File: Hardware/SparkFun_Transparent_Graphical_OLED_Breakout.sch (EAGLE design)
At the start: 35 parts, among them U1 AP3012, U2 UG-2856KLBAG01_4WSPI

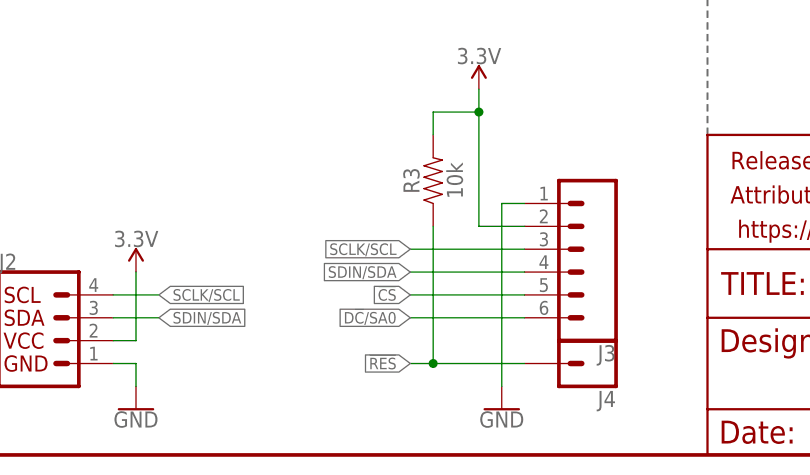
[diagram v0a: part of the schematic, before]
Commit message: Add capacitor to reset line for delayed start up!
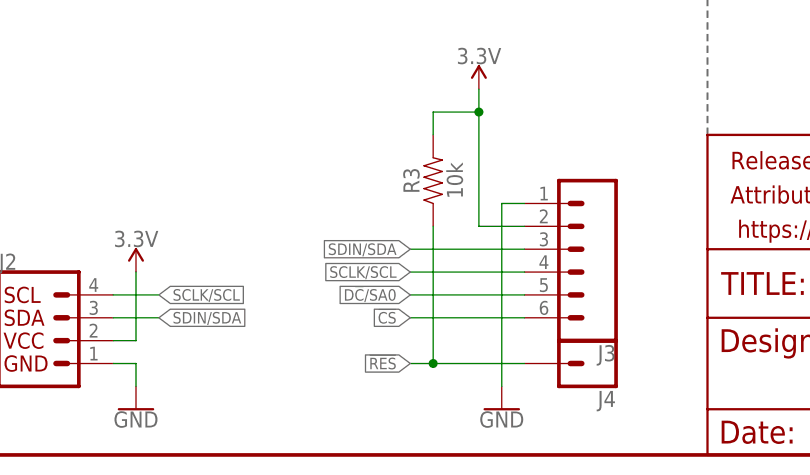
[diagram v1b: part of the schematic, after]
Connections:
- net !CS: now also J3.6; no longer J3.5
- net D!C!/SA0: now also J3.5; no longer J3.6
- net SCLK/SCL: now also J3.4; no longer J3.3
- net SDIN/SDA: now also J3.3; no longer J3.4
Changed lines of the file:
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@@
 </segment>
 <segment>
-<label x="114.3" y="17.78" size="1.27" layer="95" rot="R180" xref="yes"/>
-<pinref part="J3" gate="G$1" pin="5"/>
-<wire x1="127" y1="17.78" x2="114.3" y2="17.78" width="0.1524" layer="91"/>
+<label x="114.3" y="15.24" size="1.27" layer="95" rot="R180" xref="yes"/>
+<wire x1="127" y1="15.24" x2="114.3" y2="15.24" width="0.1524" layer="91"/>
+<pinref part="J3" gate="G$1" pin="6"/>
 </segment>
 </net>
@@
 </segment>
 <segment>
-<label x="114.3" y="22.86" size="1.27" layer="95" rot="R180" xref="yes"/>
-<pinref part="J3" gate="G$1" pin="3"/>
-<wire x1="127" y1="22.86" x2="114.3" y2="22.86" width="0.1524" layer="91"/>
+<label x="114.3" y="20.32" size="1.27" layer="95" rot="R180" xref="yes"/>
+<wire x1="127" y1="20.32" x2="114.3" y2="20.32" width="0.1524" layer="91"/>
+<pinref part="J3" gate="G$1" pin="4"/>
 </segment>
 </net>
@@
 </segment>
 <segment>
-<label x="114.3" y="20.32" size="1.27" layer="95" rot="R180" xref="yes"/>
-<pinref part="J3" gate="G$1" pin="4"/>
-<wire x1="127" y1="20.32" x2="114.3" y2="20.32" width="0.1524" layer="91"/>
+<label x="114.3" y="22.86" size="1.27" layer="95" rot="R180" xref="yes"/>
+<wire x1="127" y1="22.86" x2="114.3" y2="22.86" width="0.1524" layer="91"/>
+<pinref part="J3" gate="G$1" pin="3"/>
 </segment>
 </net>
@@
 </segment>
 <segment>
-<label x="114.3" y="15.24" size="1.27" layer="95" rot="R180" xref="yes"/>
-<pinref part="J3" gate="G$1" pin="6"/>
-<wire x1="114.3" y1="15.24" x2="127" y2="15.24" width="0.1524" layer="91"/>
+<label x="114.3" y="17.78" size="1.27" layer="95" rot="R180" xref="yes"/>
+<wire x1="114.3" y1="17.78" x2="127" y2="17.78" width="0.1524" layer="91"/>
+<pinref part="J3" gate="G$1" pin="5"/>
 </segment>
 </net>

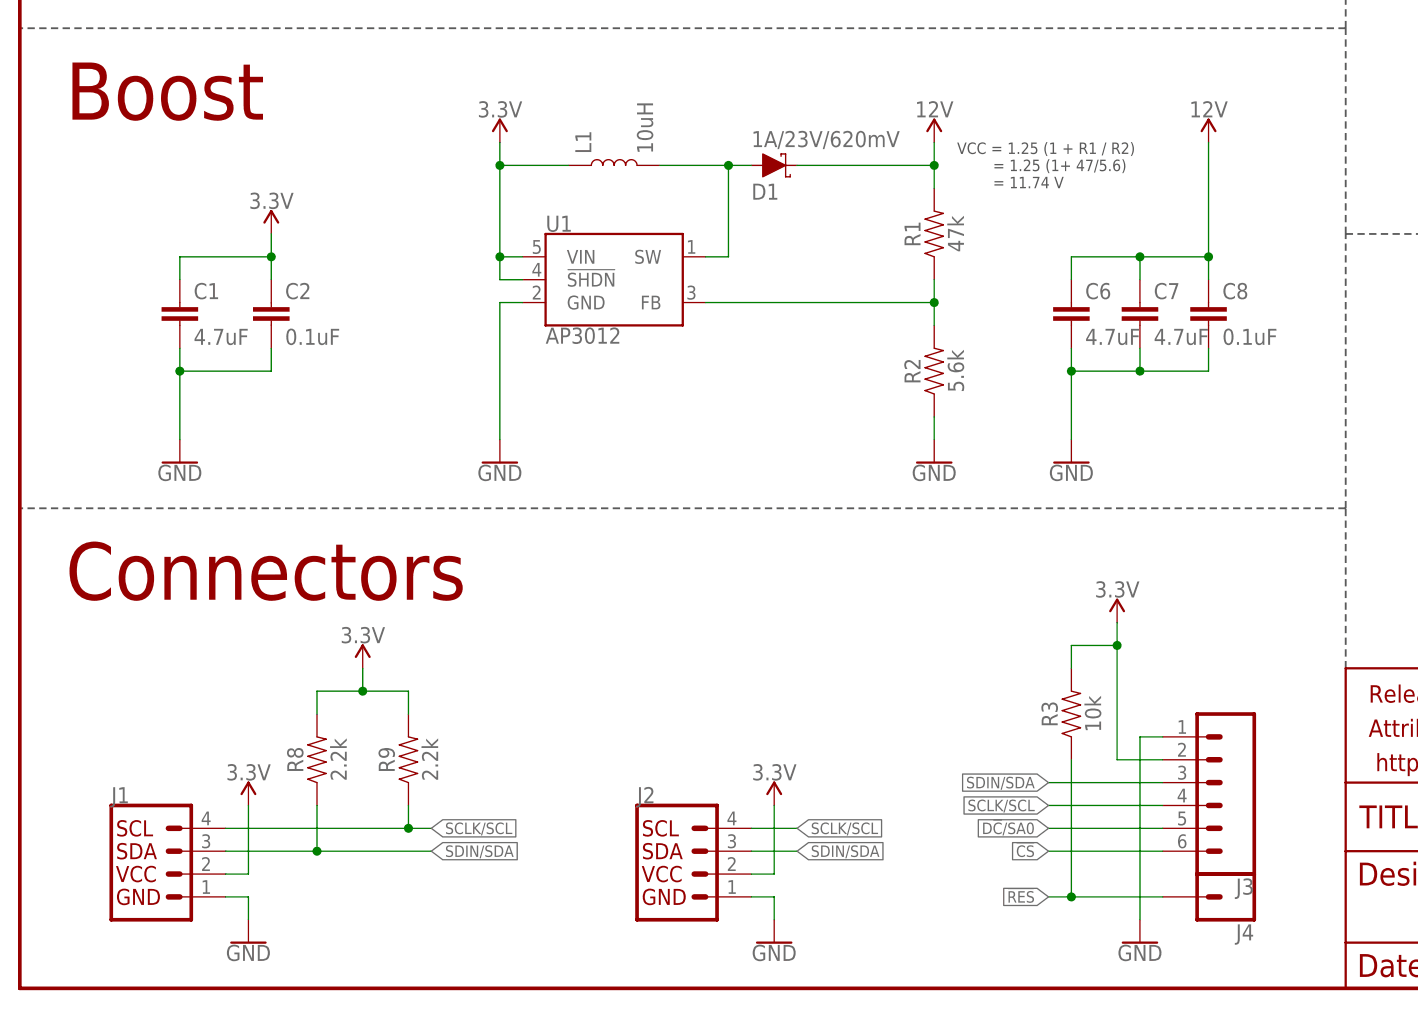
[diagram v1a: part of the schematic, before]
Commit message: Fixed proto issues
Added I2C pullup resistors and disconnect jumper, added power LED, added reset timing capacitor
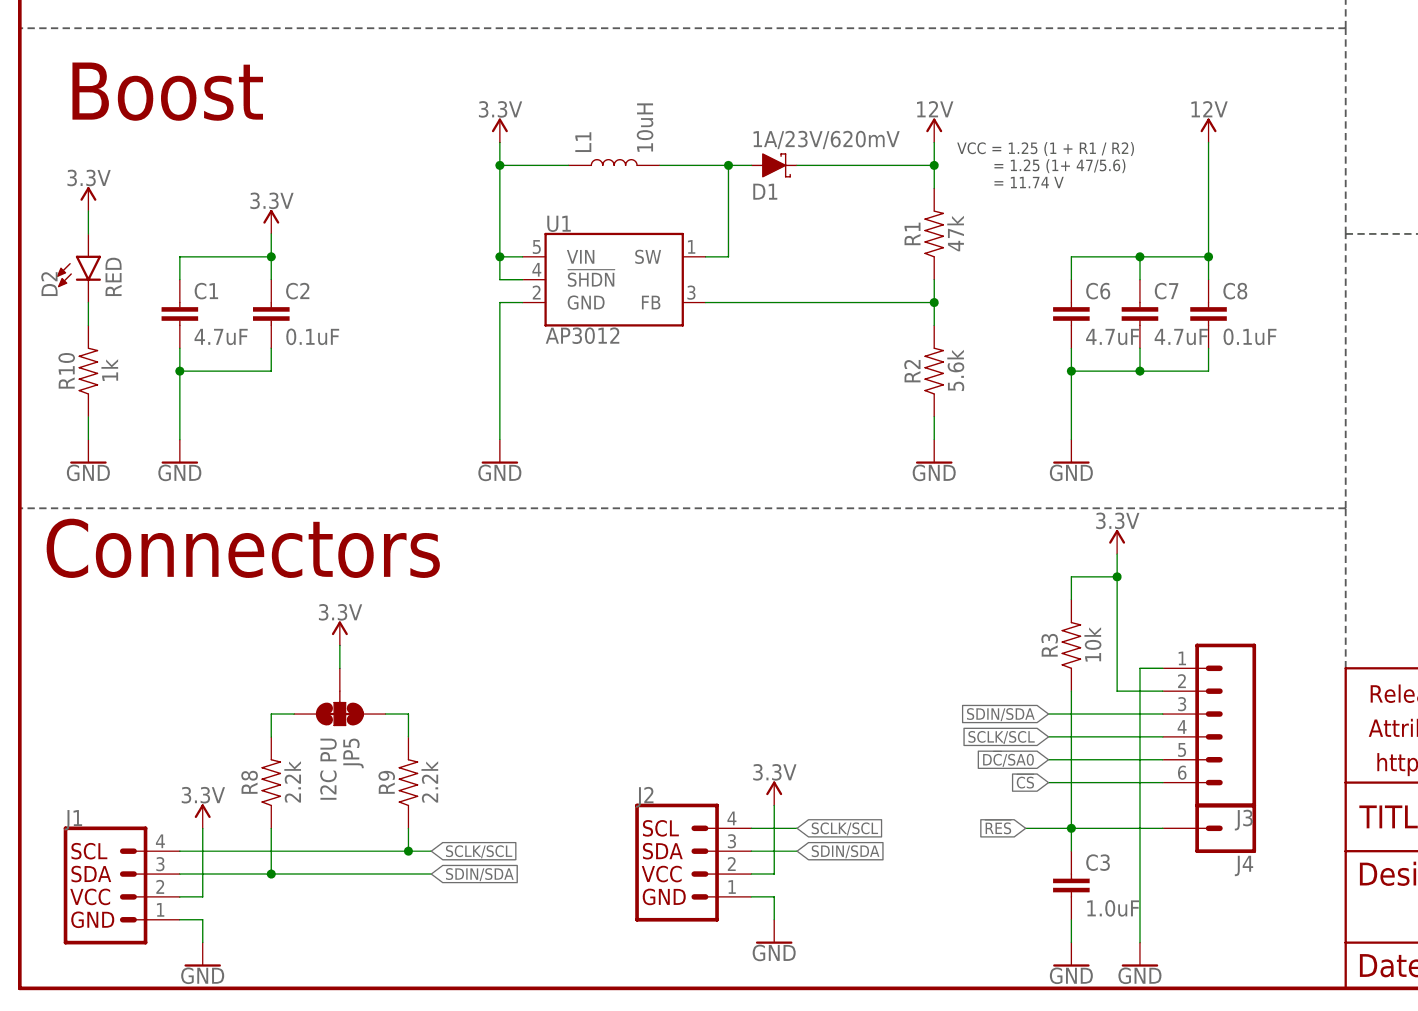
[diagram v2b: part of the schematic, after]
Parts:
- added C3: 1.0uF, SparkFun-Capacitors:1.0UF-0603-16V-10%-X7R
- added D2: RED, SparkFun-LED:LED-RED0603
- added JP5: I2C PU, SparkFun-Jumpers:JUMPER-SMT_3_2-NC_TRACE_SILK
- added R10: 1k, SparkFun-Resistors:1KOHM-0603-1/10W-1%
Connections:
- new net N$2: D2.C, R10.2
- new net N$6: JP5.3, R8.2
- new net N$7: JP5.1, R9.2
- net !RES: now also C3.1
- net 3.3V: now also D2.A, JP5.2; no longer R8.2, R9.2
- net GND: now also C3.2, R10.1
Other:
- moved on the sheet: J1, J3, J4, R3, R8, R9

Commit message: Tidy schematic
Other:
- moved on the sheet: C3
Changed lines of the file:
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@@
 <instance part="R9" gate="G$1" x="43.18" y="22.86" rot="R90"/>
 <instance part="SUPPLY13" gate="G$1" x="35.56" y="38.1"/>
-<instance part="C3" gate="G$1" x="116.84" y="10.16"/>
-<instance part="GND3" gate="1" x="116.84" y="2.54"/>
+<instance part="C3" gate="G$1" x="114.3" y="10.16"/>
+<instance part="GND3" gate="1" x="114.3" y="2.54"/>
 <instance part="D2" gate="G$1" x="7.62" y="81.28"/>
 <instance part="GND9" gate="1" x="7.62" y="58.42"/>
@@
 <pinref part="GND3" gate="1" pin="GND"/>
 <pinref part="C3" gate="G$1" pin="2"/>
-<wire x1="116.84" y1="5.08" x2="116.84" y2="7.62" width="0.1524" layer="91"/>
+<wire x1="114.3" y1="5.08" x2="114.3" y2="7.62" width="0.1524" layer="91"/>
 </segment>
 <segment>
@@
 <segment>
 <label x="111.76" y="17.78" size="1.27" layer="95" rot="R180" xref="yes"/>
-<wire x1="116.84" y1="17.78" x2="111.76" y2="17.78" width="0.1524" layer="91"/>
+<wire x1="116.84" y1="17.78" x2="114.3" y2="17.78" width="0.1524" layer="91"/>
 <pinref part="R3" gate="G$1" pin="1"/>
+<wire x1="114.3" y1="17.78" x2="111.76" y2="17.78" width="0.1524" layer="91"/>
 <wire x1="116.84" y1="33.02" x2="116.84" y2="17.78" width="0.1524" layer="91"/>
 <wire x1="116.84" y1="17.78" x2="127" y2="17.78" width="0.1524" layer="91"/>
@@
 <pinref part="J4" gate="G$1" pin="1"/>
 <pinref part="C3" gate="G$1" pin="1"/>
-<wire x1="116.84" y1="15.24" x2="116.84" y2="17.78" width="0.1524" layer="91"/>
+<wire x1="114.3" y1="15.24" x2="114.3" y2="17.78" width="0.1524" layer="91"/>
+<junction x="114.3" y="17.78"/>
 </segment>
 </net>
@@
 </segment>
 <segment>
-<label x="114.3" y="22.86" size="1.27" layer="95" rot="R180" xref="yes"/>
-<wire x1="127" y1="22.86" x2="114.3" y2="22.86" width="0.1524" layer="91"/>
+<label x="111.76" y="22.86" size="1.27" layer="95" rot="R180" xref="yes"/>
+<wire x1="127" y1="22.86" x2="111.76" y2="22.86" width="0.1524" layer="91"/>
 <pinref part="J3" gate="G$1" pin="6"/>
 </segment>
@@
 </segment>
 <segment>
-<label x="114.3" y="27.94" size="1.27" layer="95" rot="R180" xref="yes"/>
-<wire x1="127" y1="27.94" x2="114.3" y2="27.94" width="0.1524" layer="91"/>
+<label x="111.76" y="27.94" size="1.27" layer="95" rot="R180" xref="yes"/>
+<wire x1="127" y1="27.94" x2="111.76" y2="27.94" width="0.1524" layer="91"/>
 <pinref part="J3" gate="G$1" pin="4"/>
 </segment>
@@
 </segment>
 <segment>
-<label x="114.3" y="30.48" size="1.27" layer="95" rot="R180" xref="yes"/>
-<wire x1="127" y1="30.48" x2="114.3" y2="30.48" width="0.1524" layer="91"/>
+<label x="111.76" y="30.48" size="1.27" layer="95" rot="R180" xref="yes"/>
+<wire x1="127" y1="30.48" x2="111.76" y2="30.48" width="0.1524" layer="91"/>
 <pinref part="J3" gate="G$1" pin="3"/>
 </segment>
@@
 </segment>
 <segment>
-<label x="114.3" y="25.4" size="1.27" layer="95" rot="R180" xref="yes"/>
-<wire x1="114.3" y1="25.4" x2="127" y2="25.4" width="0.1524" layer="91"/>
+<label x="111.76" y="25.4" size="1.27" layer="95" rot="R180" xref="yes"/>
+<wire x1="111.76" y1="25.4" x2="127" y2="25.4" width="0.1524" layer="91"/>
 <pinref part="J3" gate="G$1" pin="5"/>
 </segment>

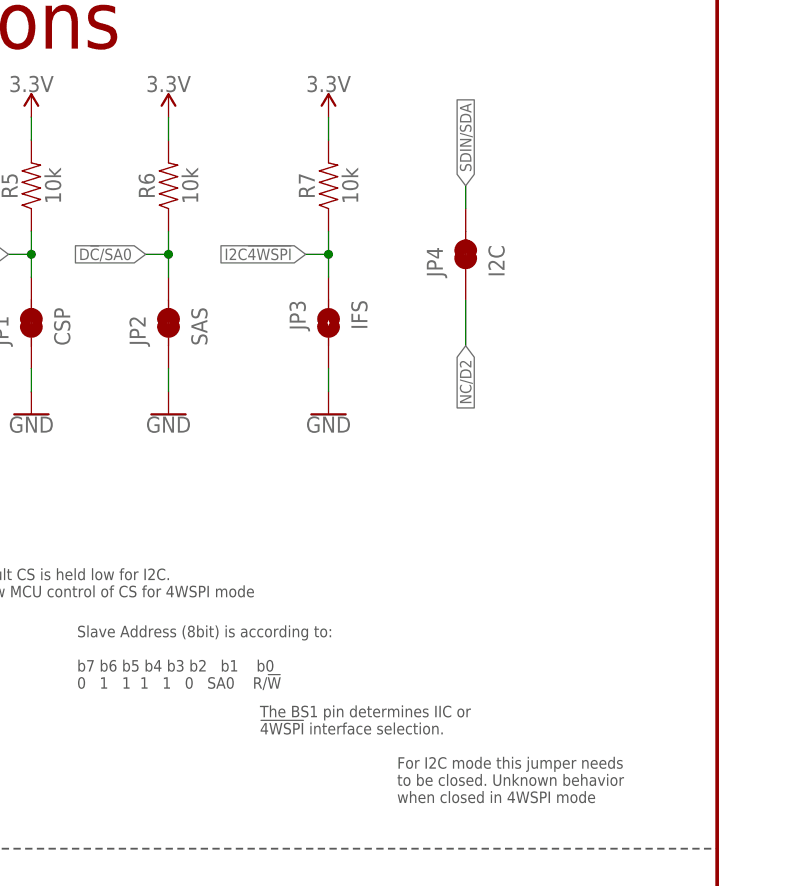
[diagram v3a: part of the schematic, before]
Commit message: Changed polarity of IFS jumper so that changing to SPI is all cutting, changed silk to match
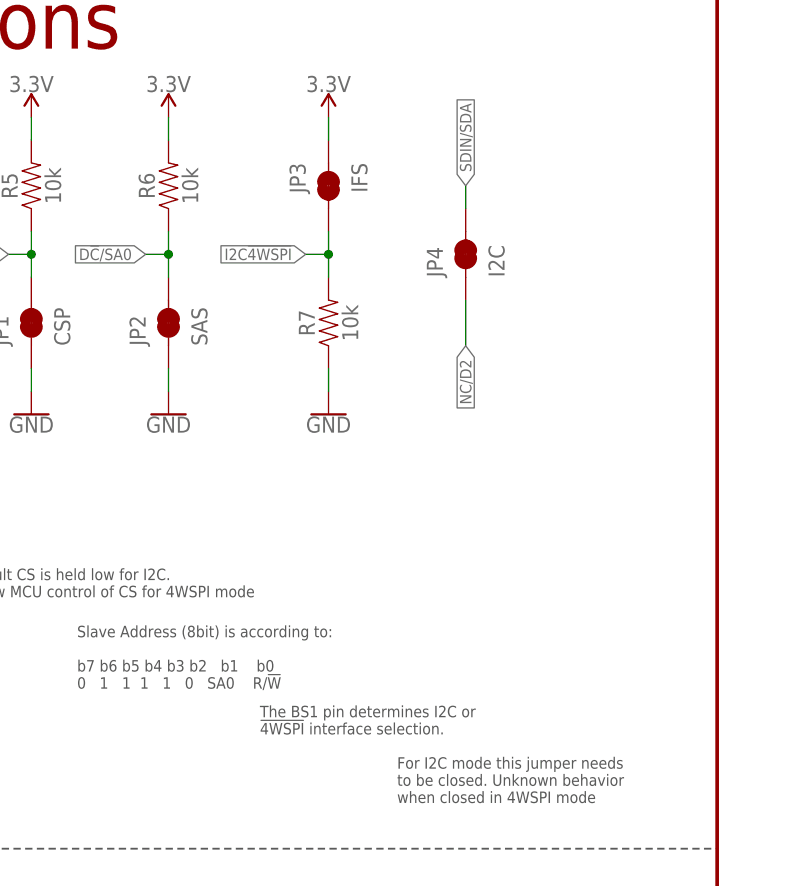
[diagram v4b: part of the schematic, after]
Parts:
- JP3: device SparkFun-Jumpers:JUMPER-SMT_2_NO_SILK -> SparkFun-Jumpers:JUMPER-SMT_2_NC_TRACE_SILK
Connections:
- net 3.3V: now also JP3.1; no longer R7.2
- net GND: now also R7.1; no longer JP3.2
- net I2C!4WSPI: now also JP3.2, R7.2; no longer JP3.1, R7.1
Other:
- note added: "The BS1 pin determines I2C or !4WSPI! interface selection."
- note removed: "The BS1 pin determines IIC or !4WSPI! interface selection."
- moved on the sheet: R7
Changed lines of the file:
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@@
 <part name="GND14" library="SparkFun-PowerSymbols" deviceset="GND" device=""/>
 <part name="SUPPLY12" library="SparkFun-PowerSymbols" deviceset="3.3V" device=""/>
-<part name="JP3" library="SparkFun-Jumpers" deviceset="JUMPER-SMT_2_NO" device="_SILK" value="IFS"/>
+<part name="JP3" library="SparkFun-Jumpers" deviceset="JUMPER-SMT_2_NC_TRACE" device="_SILK" value="IFS"/>
 <part name="JP4" library="SparkFun-Jumpers" deviceset="JUMPER-SMT_2_NC_TRACE" device="_SILK" value="I2C"/>
 <part name="SUPPLY8" library="SparkFun-PowerSymbols" deviceset="3.3V" device=""/>
@@
 b7 b6 b5 b4 b3 b2   b1    b0
 0   1   1  1   1   0   SA0    R/!W</text>
-<text x="198.12" y="96.52" size="1.27" layer="97">The BS1 pin determines IIC or
+<text x="198.12" y="96.52" size="1.27" layer="97">The BS1 pin determines I2C or
 !4WSPI! interface selection. </text>
 <text x="213.36" y="88.9" size="1.27" layer="97">For I2C mode this jumper needs
@@
 <instance part="GND13" gate="1" x="187.96" y="132.08"/>
 <instance part="SUPPLY11" gate="G$1" x="187.96" y="165.1"/>
-<instance part="R7" gate="G$1" x="205.74" y="157.48" rot="R90"/>
+<instance part="R7" gate="G$1" x="205.74" y="142.24" rot="R90"/>
 <instance part="GND14" gate="1" x="205.74" y="132.08"/>
 <instance part="SUPPLY12" gate="G$1" x="205.74" y="165.1"/>
-<instance part="JP3" gate="G$1" x="205.74" y="142.24" rot="MR270"/>
+<instance part="JP3" gate="G$1" x="205.74" y="157.48" rot="MR270"/>
 <instance part="JP4" gate="G$1" x="220.98" y="149.86" rot="R90"/>
 <instance part="SUPPLY8" gate="G$1" x="121.92" y="48.26"/>
@@
 </segment>
 <segment>
-<pinref part="GND14" gate="1" pin="GND"/>
-<pinref part="JP3" gate="G$1" pin="2"/>
-<wire x1="205.74" y1="134.62" x2="205.74" y2="137.16" width="0.1524" layer="91"/>
-</segment>
-<segment>
 <pinref part="GND3" gate="1" pin="GND"/>
 <pinref part="C3" gate="G$1" pin="2"/>
@@
 <pinref part="GND9" gate="1" pin="GND"/>
 <wire x1="7.62" y1="63.5" x2="7.62" y2="60.96" width="0.1524" layer="91"/>
+</segment>
+<segment>
+<pinref part="R7" gate="G$1" pin="1"/>
+<pinref part="GND14" gate="1" pin="GND"/>
+<wire x1="205.74" y1="137.16" x2="205.74" y2="134.62" width="0.1524" layer="91"/>
 </segment>
 </net>
@@
 </segment>
 <segment>
-<pinref part="R7" gate="G$1" pin="2"/>
-<pinref part="SUPPLY12" gate="G$1" pin="3.3V"/>
-<wire x1="205.74" y1="162.56" x2="205.74" y2="165.1" width="0.1524" layer="91"/>
-</segment>
-<segment>
 <pinref part="SUPPLY14" gate="G$1" pin="3.3V"/>
 <pinref part="D2" gate="G$1" pin="A"/>
@@
 <pinref part="JP5" gate="G$1" pin="2"/>
 <wire x1="35.56" y1="38.1" x2="35.56" y2="35.56" width="0.1524" layer="91"/>
+</segment>
+<segment>
+<pinref part="JP3" gate="G$1" pin="1"/>
+<pinref part="SUPPLY12" gate="G$1" pin="3.3V"/>
+<wire x1="205.74" y1="162.56" x2="205.74" y2="165.1" width="0.1524" layer="91"/>
 </segment>
 </net>
@@
 <net name="I2C!4WSPI" class="0">
 <segment>
-<pinref part="R7" gate="G$1" pin="1"/>
-<wire x1="205.74" y1="152.4" x2="205.74" y2="149.86" width="0.1524" layer="91"/>
 <wire x1="205.74" y1="149.86" x2="203.2" y2="149.86" width="0.1524" layer="91"/>
 <label x="203.2" y="149.86" size="1.27" layer="95" rot="R180" xref="yes"/>
-<pinref part="JP3" gate="G$1" pin="1"/>
+<pinref part="R7" gate="G$1" pin="2"/>
 <wire x1="205.74" y1="147.32" x2="205.74" y2="149.86" width="0.1524" layer="91"/>
+<pinref part="JP3" gate="G$1" pin="2"/>
+<wire x1="205.74" y1="152.4" x2="205.74" y2="149.86" width="0.1524" layer="91"/>
 <junction x="205.74" y="149.86"/>
 </segment>
